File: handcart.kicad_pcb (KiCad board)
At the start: 2 copper layers, 166 x 65 mm, 50 parts, among them J1 PANEL, J10 FANS, J2 BMS, J3 Raspberry_Pi_2_3, J4 DB9_Female_DCE, J5 CHARGER, J8 POWER, K1 OJE-SH-112DM, Q1 2N7002NXAKR, Q2 NTR5105PT1G, Q3 NTR5105PT1G, Q4 2N7002NXAKR, Q5 NTR5105PT1G, Q6 2N7002NXAKR, Q7 2N7002NXAKR, SW1 SW_SPDT, U1 MCP2515-xSO, U2 MCP2562-E-SN, U3 MAX3232CDR, U4 Tex_DCDC, U5 L7805, Y1 16MHz

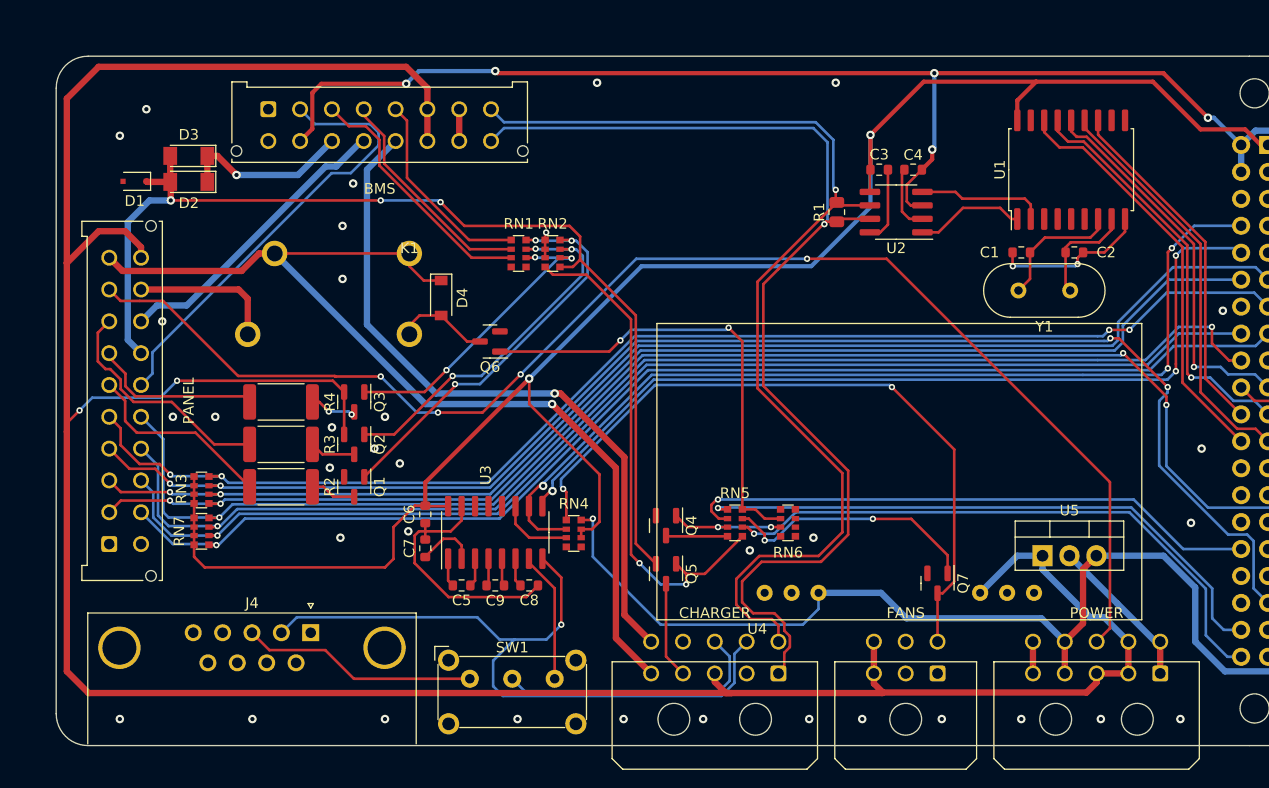
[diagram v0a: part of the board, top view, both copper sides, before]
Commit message: added mounting holes
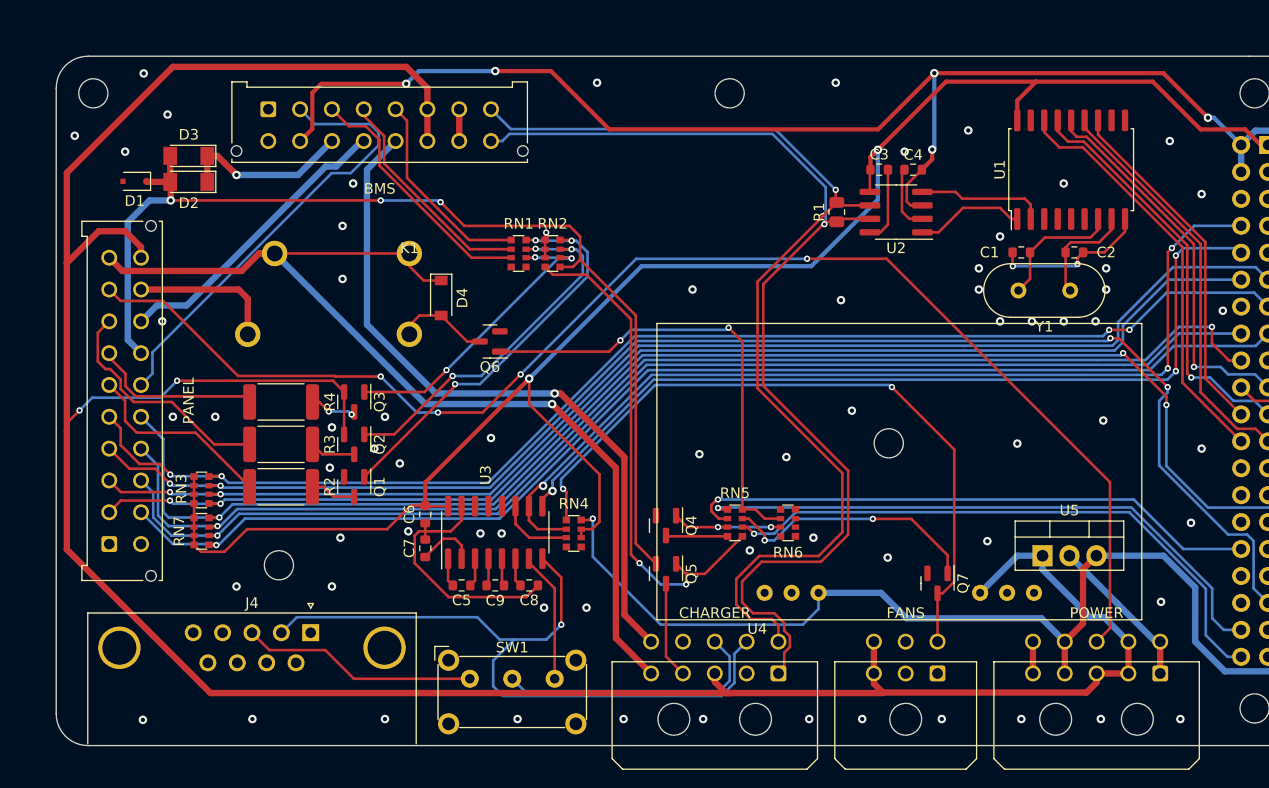
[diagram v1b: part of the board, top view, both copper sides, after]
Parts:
- added REF**: MountingHole_2.75_6.1Free, handcart:MountingHole_2.75_6.1Free, F.Cu at (180.2, 94.5)
- added REF**: MountingHole_2.75_6.1Free, handcart:MountingHole_2.75_6.1Free, F.Cu at (165.2, 61.5)
- added REF**: MountingHole_2.75_6.1Free, handcart:MountingHole_2.75_6.1Free, F.Cu at (122.7, 106.0)
- added REF**: MountingHole_2.75_6.1Free, handcart:MountingHole_2.75_6.1Free, F.Cu at (105.2, 61.5)
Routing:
- net +12V: track 270.7 -> 259.8 mm
- net +3V3: track 195.5 -> 189.5 mm
- net +5V: track 267.6 -> 272.0 mm
- net /CAN+: track 104.2 -> 101.0 mm
- net /CAN-: track 100.8 -> 98.2 mm
- net GND: vias 48 -> 81

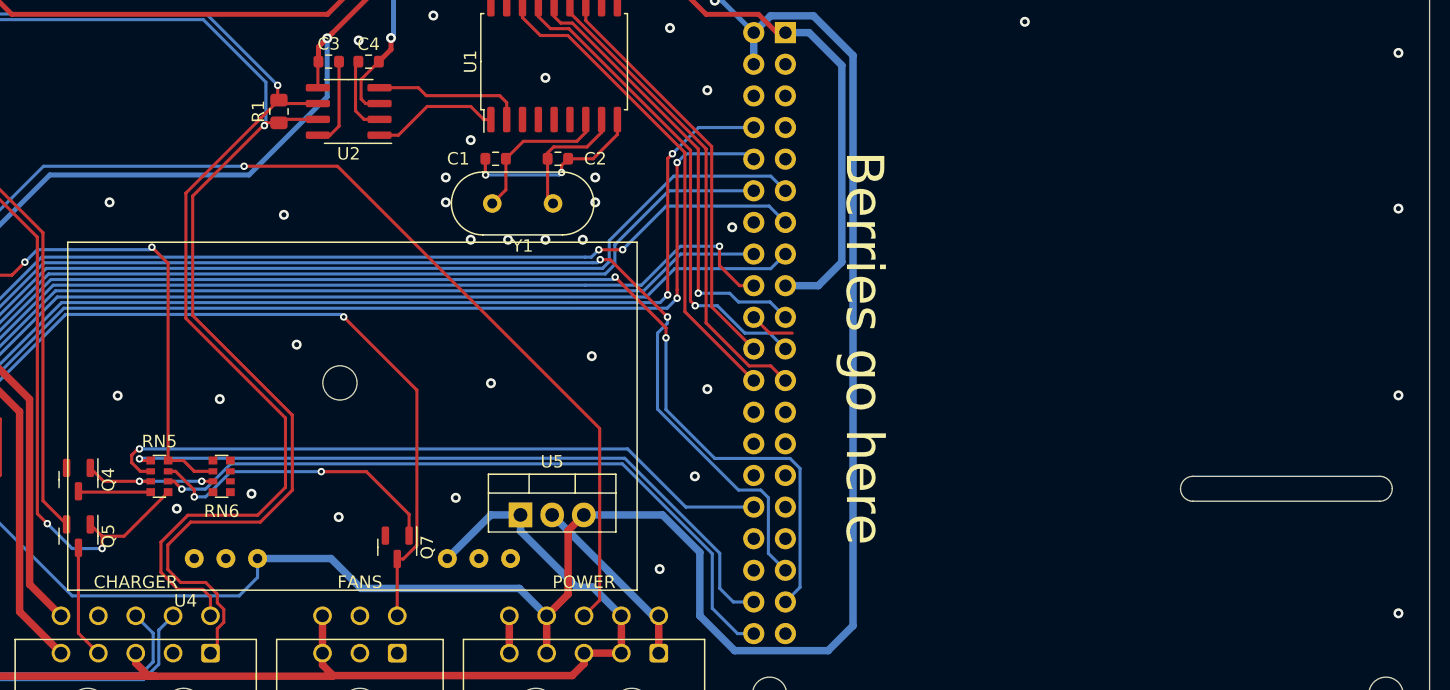
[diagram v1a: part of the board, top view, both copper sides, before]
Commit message: added fan hole to pi
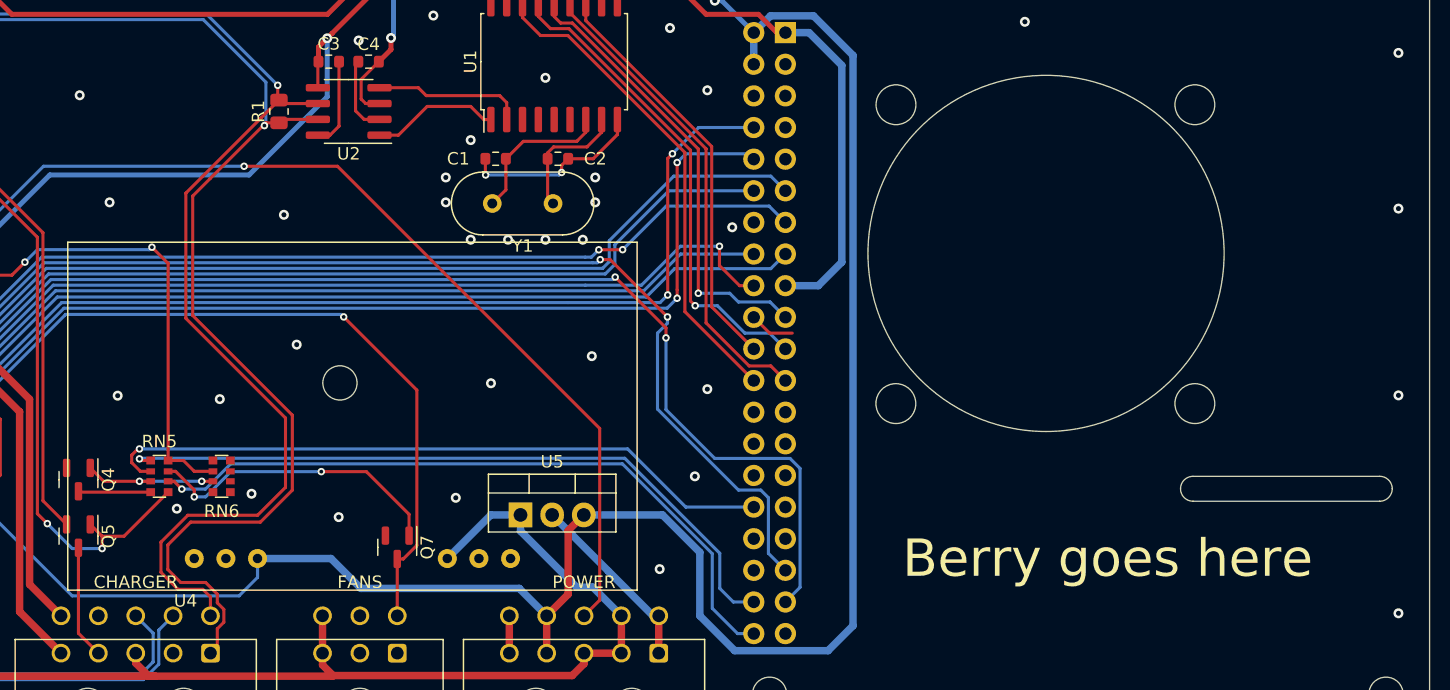
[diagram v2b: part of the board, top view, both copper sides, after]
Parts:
- removed H1, H2, H3, H4: MountingHole, handcart:MountingHole_2.75_6.1Free
- added REF**: MountingHole_3.2mm_M3_ISO14580, MountingHole:MountingHole_3.2mm_M3_ISO14580, F.Cu at (224.8, 96.2)
- added REF**: MountingHole_3.2mm_M3_ISO14580, MountingHole:MountingHole_3.2mm_M3_ISO14580, F.Cu at (248.8, 96.2)
- added REF**: MountingHole_3.2mm_M3_ISO14580, MountingHole:MountingHole_3.2mm_M3_ISO14580, F.Cu at (248.8, 72.2)
- added REF**: MountingHole_3.2mm_M3_ISO14580, MountingHole:MountingHole_3.2mm_M3_ISO14580, F.Cu at (224.8, 72.2)
- J3: footprint Connector_PinHeader_2.54mm:PinHeader_2x20_P2.54mm_Vertical -> handcart:raspberrypi_hat_template
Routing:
- net GND: vias 81 -> 82
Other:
- outline, holes or cut-outs redrawn
- board text added: "Berry goes here"
- board text removed: "Berries go here"

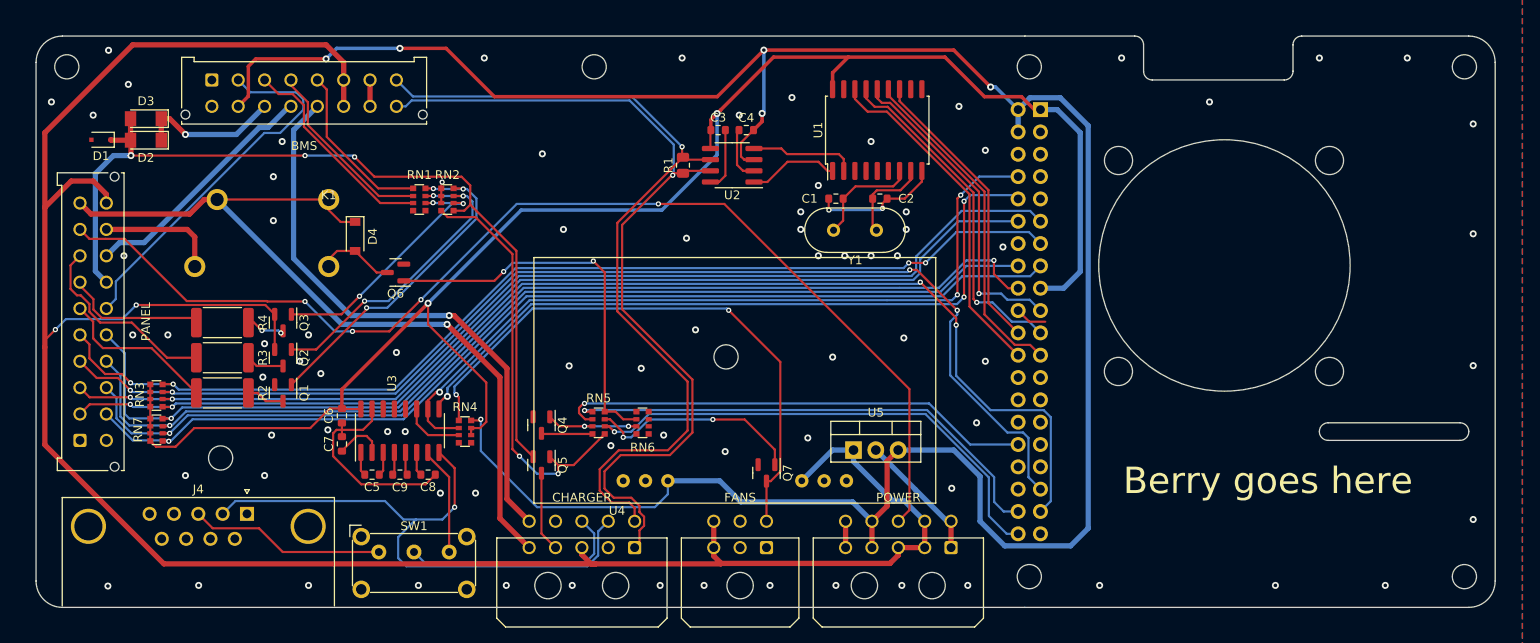
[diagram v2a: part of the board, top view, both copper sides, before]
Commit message: All mounting holes to M3
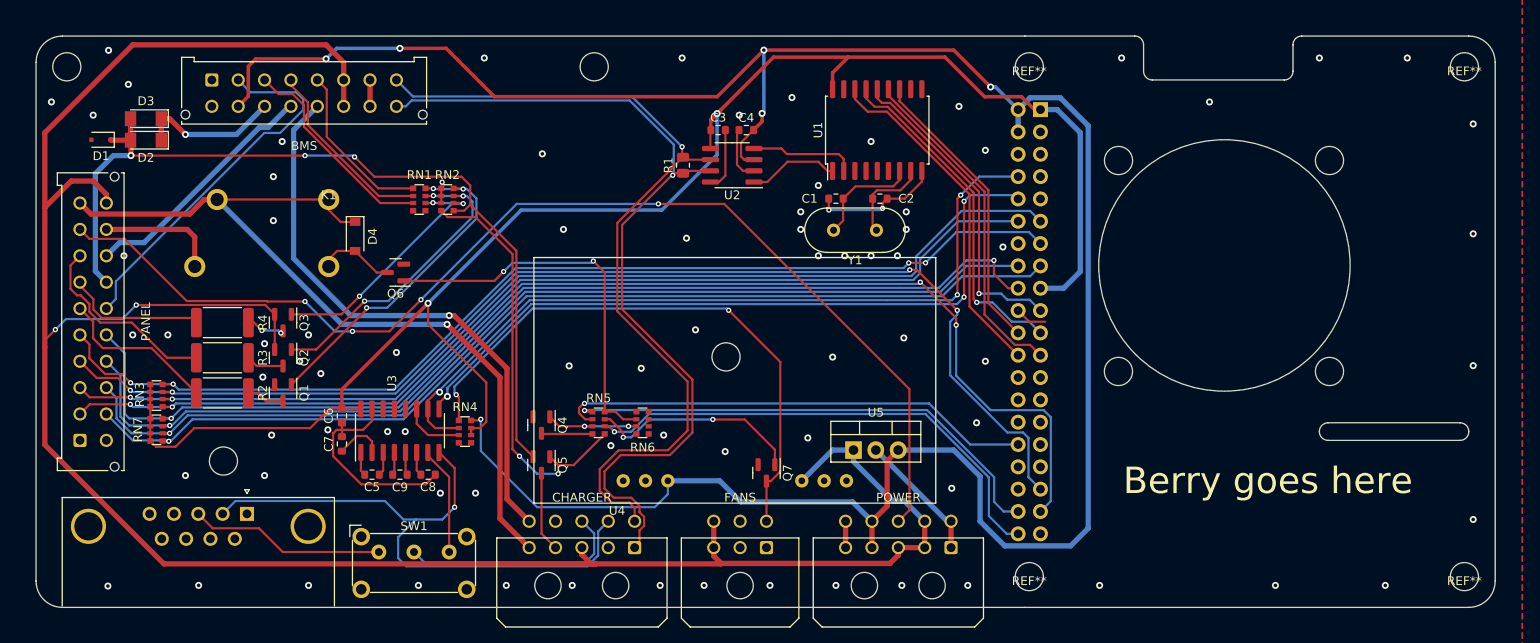
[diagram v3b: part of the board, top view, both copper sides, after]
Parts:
- added REF**: MountingHole_3.2_6.1Free, handcart:MountingHole_3.2_6.1Free, F.Cu at (214.7, 119.5)
- added REF**: MountingHole_3.2_6.1Free, handcart:MountingHole_3.2_6.1Free, F.Cu at (264.2, 119.5)
- added REF**: MountingHole_3.2_6.1Free, handcart:MountingHole_3.2_6.1Free, F.Cu at (264.2, 61.5)
- added REF**: MountingHole_3.2_6.1Free, handcart:MountingHole_3.2_6.1Free, F.Cu at (214.7, 61.5)
- REF** (x4): value MountingHole_2.75_6.1Free -> MountingHole_3.2_6.1Free; footprint handcart:MountingHole_2.75_6.1Free -> handcart:MountingHole_3.2_6.1Free
- moved REF** 0.47 mm to (123.0, 106.3)

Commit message: as printed v2
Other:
- board text added: "HANDCART"
- board text added: "v2 20210808"

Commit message: changed relay, modified gitignore, did the output
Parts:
- removed the REF** at (248.8, 96.2)
- removed the REF** at (248.8, 72.2)
- removed the REF** at (214.7, 119.5)
- removed the REF** at (264.2, 119.5)
- removed the REF** at (264.2, 61.5)
- removed the REF** at (214.7, 61.5)
- removed the REF** at (224.8, 96.2)
- K1: value OJE-SH-112DM -> EX12U1S; footprint handcart:OJE-SH-112DM -> Eagle_Main:EX12U1S
- moved J4 20.0 mm to (125.7, 132.4)
- moved J10 20.0 mm to (184.8, 136.2)
- moved J5 20.0 mm to (169.8, 136.2)
- moved J8 20.0 mm to (205.8, 136.2)
- moved SW1 20.0 mm to (140.7, 136.7)
- moved U4 17.9 mm to (182.1, 126.5)
- moved U5 17.9 mm to (195.6, 123.0)
- moved Q7 10.6 mm to (186.4, 97.2)
- moved K1 9.12 mm to (130.8, 84.7), turned to 270 degrees
- moved Q4 9.00 mm to (159.2, 93.3)
- moved Q5 9.00 mm to (159.2, 97.8)
- moved RN5 5.30 mm to (165.6, 96.7)
- moved RN6 5.30 mm to (170.6, 96.7)
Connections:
- K1 pad 1: /TO_CHARGER -> /FROM_MUSHROOM
- K1 pad 4: /FROM_MUSHROOM -> /TO_CHARGER
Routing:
- net GND: track 79.1 -> 125.9 mm, vias 82 -> 107
- net /PON: track 9.13 -> 38.1 mm
- net /PS_ON: track 129.5 -> 151.7 mm, vias 4 -> 5
- net +12V: track 259.8 -> 280.8 mm
- net /RASP_TX_RS232: track 12.3 -> 32.3 mm
- net /FAN_PWM: track 66.4 -> 86.1 mm
- net /FROM_CHARGER: track 66.3 -> 83.4 mm
- net /TO_CHARGER: track 95.6 -> 110.9 mm
- net /CAN+: track 101.0 -> 115.7 mm
- net /CAN-: track 98.2 -> 111.7 mm
- net Net-(Q5-Pad1): track 47.8 -> 34.8 mm, vias 2 -> 0
- net /FROM_TSMS: track 100.3 -> 90.9 mm
- net /FROM_MUSHROOM: track 13.8 -> 23.0 mm
- net +5V: track 272.0 -> 277.1 mm
- net Net-(Q6-Pad1): track 44.1 -> 39.3 mm
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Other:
- board size 166 x 65 mm -> 166 x 85 mm
- board text added: "v2 20211111"
- board text removed: "Move: X210,Y130,R270"
- board text removed: "v2 20210808"
